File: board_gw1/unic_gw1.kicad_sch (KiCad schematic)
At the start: 127 parts, among them Q1 2N7002, Q10 2N7002, Q11 2N7002, Q12 2N7002, Q13 2N7002, Q14 2N7002, Q15 2N7002, Q16 2N7002, Q17 2N7002, Q18 2N7002, Q19 2N7002, Q2 2N7002, Q20 2N7002, Q21 2N7002, Q22 2N7002, Q23 2N7002, Q24 2N7002, Q25 2N7002, Q26 2N7002, Q27 2N7002, Q28 2N7002, Q29 2N7002, Q3 2N7002, Q30 2N7002, Q31 2N7002, Q32 2N7002, Q33 2N7002, Q34 2N7002, Q35 2N7002, Q36 2N7002, Q37 2N7002, Q38 2N7002, Q39 2N7002, Q4 2N7002, Q40 2N7002, Q41 2N7002, Q5 2N7002, Q6 2N7002, Q7 2N7002, Q8 2N7002, Q9 2N7002, U1 GW1N-LV9QN88C6_I5_, U3 MIC5203-3.3BM5, U4 APS6404L-3SQR-ZR, U5 MIC5504-1.2YM5, U6 AP62150Z6, U7 W25Q16JVUXIQ, X1 27MHz

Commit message: Fixed some footprints, fab drawings.
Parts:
- C1, C10, C11, C13, C14, C15, C16, C17, C18, C19, C2, C20, C21, C22, C23, C3, C4, C6, C9: manf YAGEO -> (none); manf# CC0402MRX5R6BB225 -> (none); manufacturer (none) -> YAGEO; mpn (none) -> CC0402MRX5R6BB225
- C5: manf Samsung Electro-Mechanics -> (none); manf# CL21A106KAYNNNG -> (none); manufacturer (none) -> Samsung Electro-Mechanics; mpn (none) -> CL21A106KAYNNNG
- C7, C8: manf Samsung Electro-Mechanics -> (none); manf# CL21A226MQQNNNE -> (none); manufacturer (none) -> Samsung Electro-Mechanics; mpn (none) -> CL21A226MQQNNNE
- D1, D11, D2, D3, D4, D5, D6, D7, D8, D9: manf SMC Diode Solutions -> (none); manf# BAT54DF -> (none); manufacturer (none) -> SMC Diode Solutions; mpn (none) -> BAT54DF
- D21, D22, D23, D24, D25, D26, D27, D28, D29, D30: manf Nexperia USA Inc. -> (none); manf# BAT54CV\,115 -> (none); manufacturer (none) -> Nexperia USA Inc.; mpn (none) -> BAT54CV\,115
- DISPLAY1: manf Crystalfontz America, Inc. -> (none); manf# CFAL12832C-0091B-W_A -> (none); manufacturer (none) -> Crystalfontz America, Inc.; mpn (none) -> CFAL12832C-0091B-W_A
- J_DISPLAY1: manf Cvilux USA -> (none); manf# CF31121D0R0-05-NH -> (none); manufacturer (none) -> Cvilux USA; mpn (none) -> CF31121D0R0-05-NH
- J_EXT1: manf Molex -> (none); manf# 502598-2793 -> (none); manufacturer (none) -> Molex; mpn (none) -> 502598-2793
- J_JTAG1: manf Amphenol ICC (FCI) -> (none); manf# 10152265-1121HF -> (none); manufacturer (none) -> Amphenol ICC (FCI); mpn (none) -> 10152265-1121HF
- L1: manf TAI-TECH Advanced Electronics Co., Ltd. -> (none); manf# UHP 252012BF-100M -> (none); manufacturer (none) -> TAI-TECH Advanced Electronics Co., Ltd.; mpn (none) -> UHP 252012BF-100M
- LED_DONE1: manf ChromeLED -> (none); manf# CS42C-QL4 -> (none); manufacturer (none) -> ChromeLED; mpn (none) -> CS42C-QL4
- Q1, Q10, Q11, Q12, Q13, Q14, Q15, Q16, Q17, Q18, Q19, Q2, Q20, Q21, Q22, Q23, Q24, Q25, Q26, Q27, Q28, Q29, Q3, Q30, Q31, Q32, Q33, Q34, Q35, Q36, Q37, Q38, Q39, Q4, Q40, Q41, Q5, Q6, Q7, Q8, Q9: manf Micro Commercial Co -> (none); manf# 2N7002KL3A-TP -> (none); manufacturer (none) -> Micro Commercial Co; mpn (none) -> 2N7002KL3A-TP
- R1: manf Bourns Inc. -> (none); manf# CR0402-JW-221GLF -> (none); manufacturer (none) -> Bourns Inc.; mpn (none) -> CR0402-JW-221GLF
- R10, R11, R12, R13, R15, R16, R17, R3, R5, R6, R7, R8, R9: manf Bourns Inc. -> (none); manf# CR0402-FX-1002GLF -> (none); manufacturer (none) -> Bourns Inc.; mpn (none) -> CR0402-FX-1002GLF
- R14: manf Bourns Inc. -> (none); manf# CR0402-FX-4991GLF -> (none); manufacturer (none) -> Bourns Inc.; mpn (none) -> CR0402-FX-4991GLF
- R2: manf Bourns Inc. -> (none); manf# CR0402-JW-102GLF -> (none); manufacturer (none) -> Bourns Inc.; mpn (none) -> CR0402-JW-102GLF
- R4: manf Bourns Inc. -> (none); manf# CR0402-FX-3162GLF -> (none); manufacturer (none) -> Bourns Inc.; mpn (none) -> CR0402-FX-3162GLF
- SOCKET1: manf Batten & Allen Limited -> (none); manf# BA3760-TUBL-4A-F5 -> (none); manufacturer (none) -> Batten & Allen Limited; mpn (none) -> BA3760-TUBL-4A-F5; now left out of the parts list
- TP1, TP2, TP3, TP4: now left out of the parts list
- U1: manf GOWIN Semiconductor -> (none); manf# GW1N-LV9QN88C6/I5 -> (none); manufacturer (none) -> GOWIN Semiconductor; mpn (none) -> GW1N-LV9QN88C6/I5
- U3: manf Microchip Technology -> (none); manf# MIC5203-3.3YM5-TR -> (none); manufacturer (none) -> Microchip Technology; mpn (none) -> MIC5203-3.3YM5-TR
- U4: manf AP Memory -> (none); manf# APS6404L-3SQR-ZR -> (none); manufacturer (none) -> AP Memory; mpn (none) -> APS6404L-3SQR-ZR
- U5: manf Microchip Technology -> (none); manf# MIC5504-1.2YM5-TR -> (none); manufacturer (none) -> Microchip Technology; mpn (none) -> MIC5504-1.2YM5-TR
- U6: manf Diodes Incorporated -> (none); manf# AP62150Z6-7 -> (none); manufacturer (none) -> Diodes Incorporated; mpn (none) -> AP62150Z6-7
- U7: manf Winbond Electronics -> (none); manf# W25Q16JVUXIQ TR -> (none); manufacturer (none) -> Winbond Electronics; mpn (none) -> W25Q16JVUXIQ TR
- X1: manf Jauch Quartz -> (none); manf# O 27\,0-JO32-B-1V3-1-T1-LF -> (none); manufacturer (none) -> Jauch Quartz; mpn (none) -> O 27\,0-JO32-B-1V3-1-T1-LF

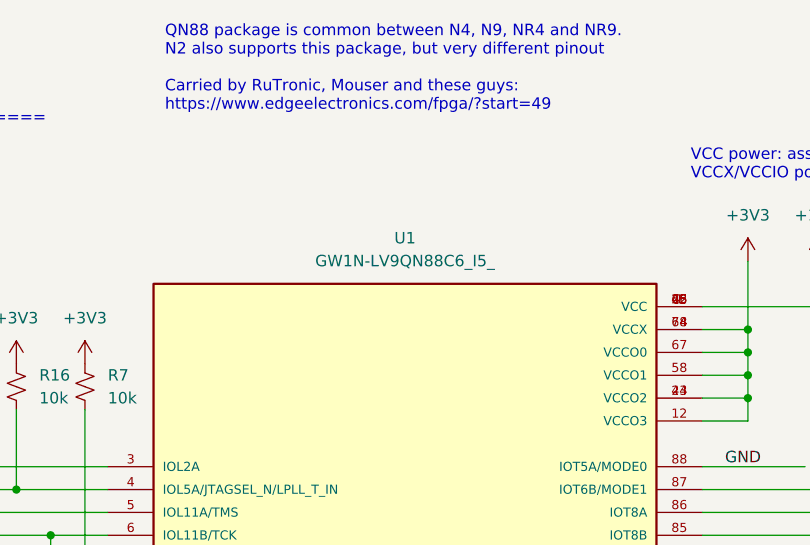
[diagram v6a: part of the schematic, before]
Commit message: Fixed GoWin part number
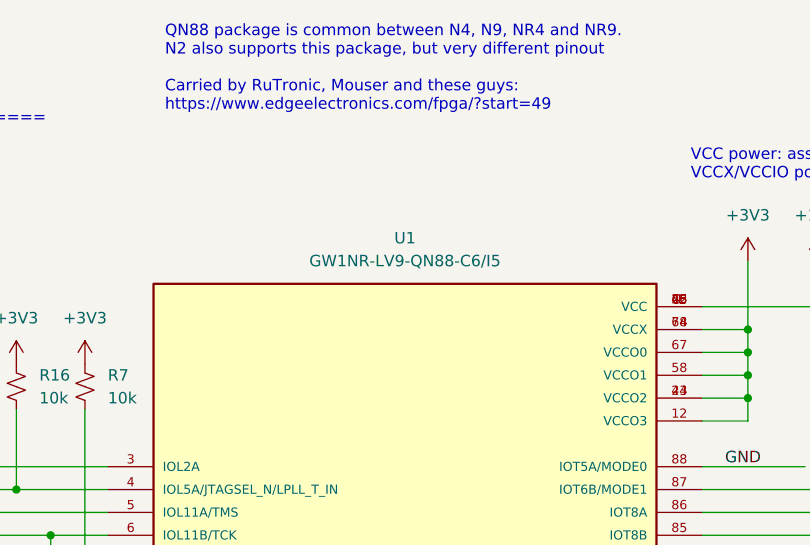
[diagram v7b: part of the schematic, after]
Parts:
- U1: value GW1N-LV9QN88C6_I5_ -> GW1NR-LV9-QN88-C6/I5; MP GW1N-LV9QN88C6/I5/ -> (none); SnapEDA_Link https://www.snapeda.com/parts/GW1N-LV9QN88C6/I5//Gowin+Semi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 -> (none); mpn GW1N-LV9QN88C6/I5 -> GW1NR-LV9-QN88-C6/I5
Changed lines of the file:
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@@
 			)
 		)
-		(property "Value" "GW1N-LV9QN88C6_I5_"
+		(property "Value" "GW1NR-LV9-QN88-C6/I5"
 			(at 166.37 45.72 0)
 			(effects
@@
 			)
 		)
-		(property "Datasheet" "https://www.digikey.com/en/models/776031"
+		(property "Datasheet" ""
 			(at 166.37 109.22 0)
 			(effects
@@
 			)
 		)
-		(property "SnapEDA_Link" "https://www.snapeda.com/parts/GW1N-LV9QN88C6/I5//Gowin+Semiconductor/view-part/?ref=snap"
-			(at 166.37 109.22 0)
-			(effects
-				(font
-					(size 1.27 1.27)
-				)
-				(justify bottom)
-				(hide yes)
-			)
-		)
-		(property "MP" "GW1N-LV9QN88C6/I5/"
-			(at 166.37 109.22 0)
-			(effects
-				(font
-					(size 1.27 1.27)
-				)
-				(justify bottom)
-				(hide yes)
-			)
-		)
 		(property "Availability" "Not in stock"
 			(at 166.37 109.22 0)
@@
 			)
 		)
-		(property "mpn" "GW1N-LV9QN88C6/I5"
+		(property "mpn" "GW1NR-LV9-QN88-C6/I5"
 			(at 166.37 109.22 0)
 			(effects

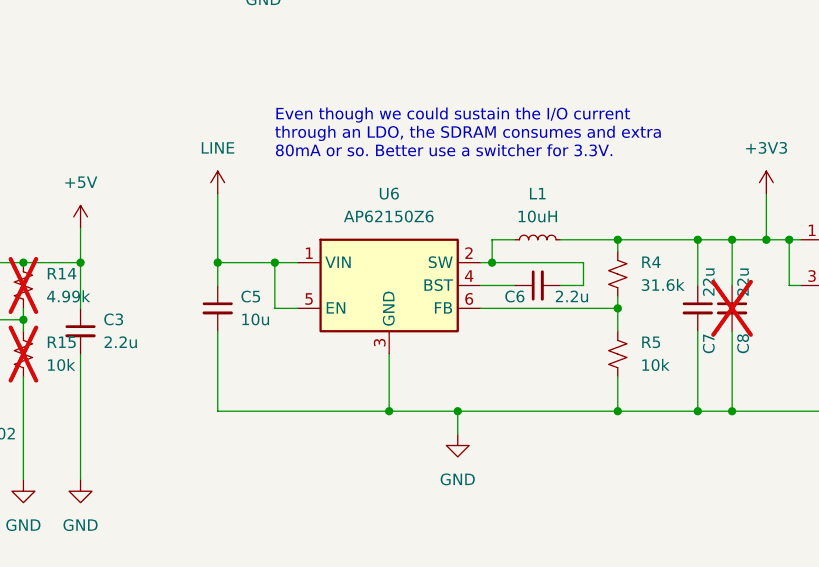
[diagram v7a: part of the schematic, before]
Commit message: ECO for switcher part change
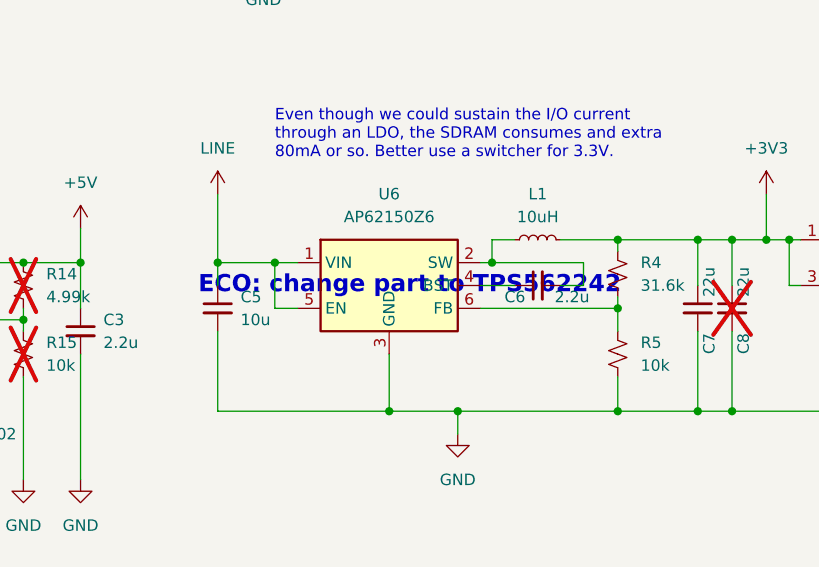
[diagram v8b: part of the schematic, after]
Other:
- note added: "ECO: change part to TPS562242"
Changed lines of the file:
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@@
+		)
+	)
+	(text "ECO: change part to TPS562242"
+		(exclude_from_sim no)
+		(at 206.756 264.16 0)
+		(effects
+			(font
+				(size 1.905 1.905)
+				(thickness 0.762)
+				(bold yes)
+				(color 255 0 0 1)
+			)
 		)
 	)
